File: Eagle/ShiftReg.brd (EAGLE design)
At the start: 100 x 100 mm, 206 parts, among them Q10 310mA/60V/1.6Ω, Q100 310mA/60V/1.6Ω, Q101 310mA/60V/1.6Ω, Q102 310mA/60V/1.6Ω, Q103 310mA/60V/1.6Ω, Q104 310mA/60V/1.6Ω, Q105 310mA/60V/1.6Ω, Q106 310mA/60V/1.6Ω, Q107 310mA/60V/1.6Ω, Q108 310mA/60V/1.6Ω, Q109 310mA/60V/1.6Ω, Q11 310mA/60V/1.6Ω, Q110 310mA/60V/1.6Ω, Q111 310mA/60V/1.6Ω, Q112 310mA/60V/1.6Ω, Q113 310mA/60V/1.6Ω, Q114 310mA/60V/1.6Ω, Q115 310mA/60V/1.6Ω, Q116 310mA/60V/1.6Ω, Q117 310mA/60V/1.6Ω, Q118 310mA/60V/1.6Ω, Q119 310mA/60V/1.6Ω, Q12 310mA/60V/1.6Ω, Q120 310mA/60V/1.6Ω, Q121 310mA/60V/1.6Ω, Q122 310mA/60V/1.6Ω, Q123 310mA/60V/1.6Ω, Q124 310mA/60V/1.6Ω, Q125 310mA/60V/1.6Ω, Q126 310mA/60V/1.6Ω, Q127 310mA/60V/1.6Ω, Q128 310mA/60V/1.6Ω, Q129 310mA/60V/1.6Ω, Q13 310mA/60V/1.6Ω, Q130 310mA/60V/1.6Ω, Q131 310mA/60V/1.6Ω, Q132 310mA/60V/1.6Ω, Q133 310mA/60V/1.6Ω, Q134 310mA/60V/1.6Ω, Q135 310mA/60V/1.6Ω, Q136 310mA/60V/1.6Ω, Q137 310mA/60V/1.6Ω, Q138 310mA/60V/1.6Ω, Q139 310mA/60V/1.6Ω, Q14 310mA/60V/1.6Ω, Q140 310mA/60V/1.6Ω, Q141 310mA/60V/1.6Ω, Q142 310mA/60V/1.6Ω, Q143 310mA/60V/1.6Ω, Q144 310mA/60V/1.6Ω, Q145 310mA/60V/1.6Ω, Q146 310mA/60V/1.6Ω, Q147 310mA/60V/1.6Ω, Q148 310mA/60V/1.6Ω, Q149 310mA/60V/1.6Ω, Q15 310mA/60V/1.6Ω, Q150 310mA/60V/1.6Ω, Q151 310mA/60V/1.6Ω, Q152 310mA/60V/1.6Ω, Q153 310mA/60V/1.6Ω, Q154 310mA/60V/1.6Ω, Q155 310mA/60V/1.6Ω, Q156 310mA/60V/1.6Ω, Q157 310mA/60V/1.6Ω, Q158 310mA/60V/1.6Ω, Q159 310mA/60V/1.6Ω, Q16 310mA/60V/1.6Ω, Q160 310mA/60V/1.6Ω, Q161 310mA/60V/1.6Ω, Q162 310mA/60V/1.6Ω, Q163 310mA/60V/1.6Ω, Q164 310mA/60V/1.6Ω, Q165 310mA/60V/1.6Ω, Q25 310mA/60V/1.6Ω, Q26 310mA/60V/1.6Ω, Q27 310mA/60V/1.6Ω, Q28 310mA/60V/1.6Ω, Q29 310mA/60V/1.6Ω, Q30 310mA/60V/1.6Ω, Q31 310mA/60V/1.6Ω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

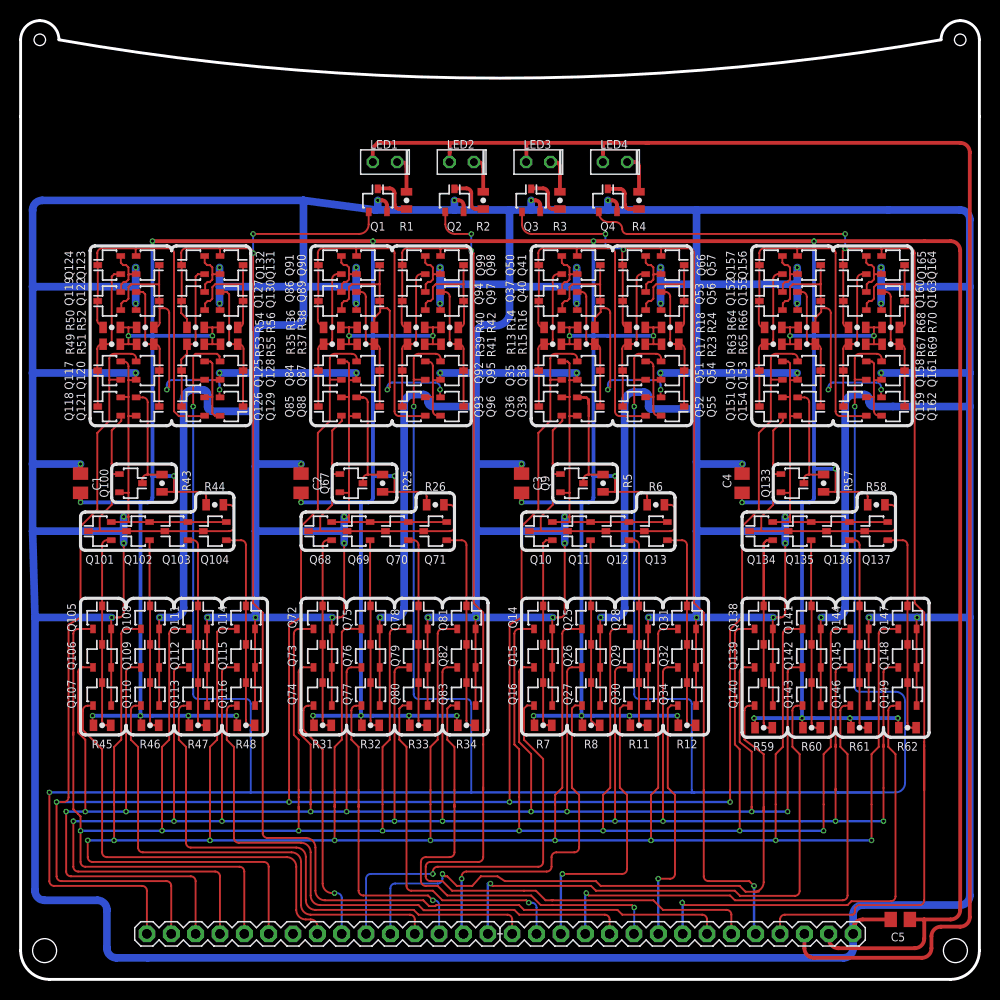
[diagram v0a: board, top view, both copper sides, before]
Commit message: Added clear to ShiftReg
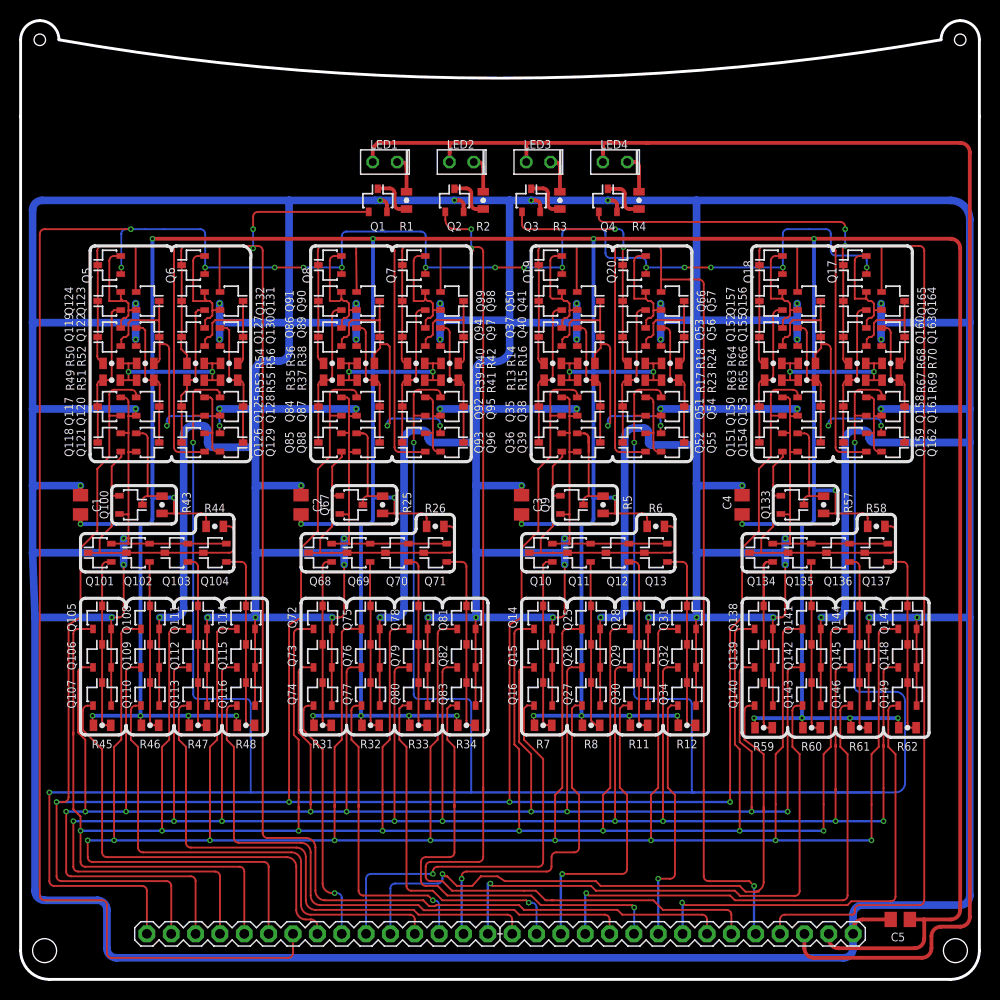
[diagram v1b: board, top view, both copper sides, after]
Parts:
- added Q17, Q18, Q19, Q20, Q5, Q6, Q7, Q8: 310mA/60V/1.6Ω, XSNOR:SOT23
- moved Q117 3.75 mm to (9.25, 59.5)
- moved Q118 3.75 mm to (9.25, 55.8)
- moved Q119 3.75 mm to (9.25, 66.8)
- moved Q120 3.75 mm to (13.2, 59.5)
- moved Q121 3.75 mm to (13.2, 55.8)
- moved Q122 3.75 mm to (13.2, 66.8)
- moved Q123 3.75 mm to (13.2, 70.5)
- moved Q124 3.75 mm to (9.25, 70.5)
- moved Q125 3.75 mm to (18.0, 59.5)
- moved Q126 3.75 mm to (18.0, 55.8)
- moved Q127 3.75 mm to (18.0, 66.8)
- moved Q128 3.75 mm to (22.0, 59.5)
- moved Q129 3.75 mm to (22.0, 55.8)
- moved Q130 3.75 mm to (22.0, 66.8)
- moved Q131 3.75 mm to (22.0, 70.5)
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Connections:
- new net CLR: JP2.7, Q17.1, Q18.1, Q19.1, Q20.1, Q5.1, Q6.1, Q7.1, Q8.1
- net GND: now also Q17.2, Q18.2, Q19.2, Q20.2, Q5.2, Q6.2, Q7.2, Q8.2
- net N$100: now also Q5.3
- net N$104: now also Q8.3
- net N$112: now also Q19.3
- net N$115: now also Q18.3
- net OUT0: now also Q6.3
- net OUT1: now also Q7.3
- net OUT2: now also Q20.3
- net OUT3: now also Q17.3
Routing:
- net CLR: track 0.00 -> 224.4 mm, vias 0 -> 15
- net GND: track 1333.8 -> 1354.1 mm
- net CLK: track 339.8 -> 324.8 mm
- net /CLK: track 308.0 -> 293.0 mm
- net N$112: track 37.4 -> 49.7 mm
- net N$104: track 37.4 -> 49.4 mm
- net N$100: track 37.4 -> 49.4 mm
- net N$115: track 37.3 -> 49.3 mm
- net OUT0: track 147.8 -> 157.4 mm
- net OUT1: track 129.7 -> 138.7 mm
- net OUT2: track 107.2 -> 112.5 mm
- net PREV3A': track 28.6 -> 24.1 mm
- net OUT3: track 136.0 -> 140.1 mm
- net R2A: track 15.1 -> 12.5 mm
- net PREV1A': track 20.6 -> 18.3 mm
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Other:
- board text added: "Clr"

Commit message: Shiftreg pcb have its own inverters for control signals
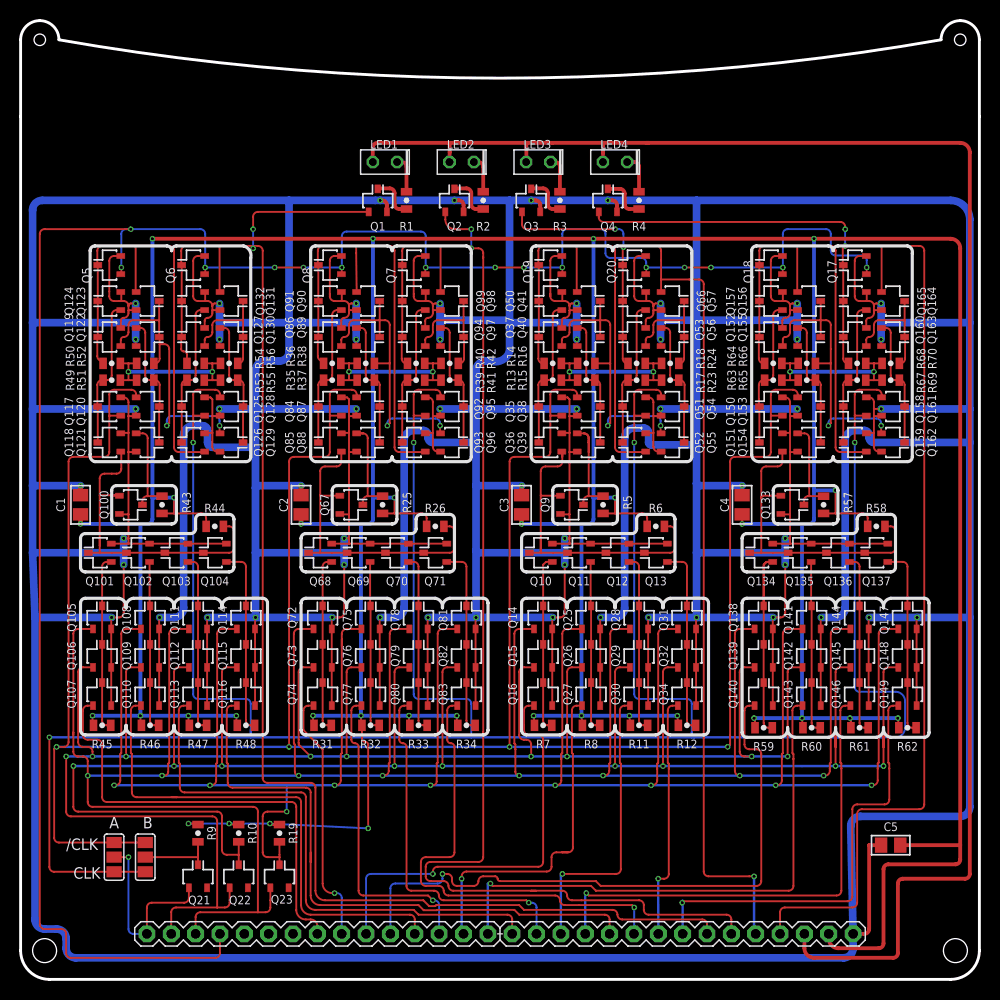
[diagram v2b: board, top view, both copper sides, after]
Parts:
- added Q21, Q22, Q23: 310mA/60V/1.6Ω, XSNOR:SOT23
- added R10, R19, R9: (no value), XSNOR:0805
- added SJ1, SJ2: (no value), jumper:SJ_2
- moved C5 7.81 mm to (90.8, 13.8)
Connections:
- new net CLK_IN: JP2.1, Q21.1, SJ2.2
- new net N$3: Q21.3, R9.1, SJ1.2
- net /CLK: now also SJ1.3, SJ2.3; no longer JP2.2
- net /OP1: now also Q22.3, R10.1; no longer JP2.4
- net /OP2: now also Q23.3, R19.1; no longer JP2.6
- net CLK: now also SJ1.1, SJ2.1; no longer JP2.1
- net CLR: now also JP2.4; no longer JP2.7
- net GND: now also Q21.2, Q22.2, Q23.2
- net OP1: now also JP2.2, Q22.1; no longer JP2.3
- net OP2: now also JP2.3, Q23.1; no longer JP2.5
- net VCC: now also R10.2, R19.2, R9.2
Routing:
- net /OP2: track 303.5 -> 241.0 mm
- net /OP1: track 250.3 -> 211.3 mm
- net VCC: track 597.2 -> 635.4 mm, vias 36 -> 40
- net OP1: track 233.8 -> 204.0 mm
- net OP2: track 289.9 -> 260.1 mm
- net CLK: track 324.8 -> 301.0 mm
- net /CLK: track 293.0 -> 271.1 mm
- net CLK_IN: track 0.00 -> 19.7 mm, vias 0 -> 1
- net N$3: track 0.00 -> 7.90 mm
- net CLR: track 224.4 -> 216.8 mm
- net GND: track 1354.1 -> 1360.6 mm
- net S2A: track 30.9 -> 34.8 mm
- net S0A-: track 30.9 -> 34.3 mm
- net S3A: track 30.9 -> 32.8 mm
- net S1A: track 30.9 -> 32.8 mm
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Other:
- board text added: "/CLK"
- board text added: "A"
- board text added: "B"
- board text added: "CLK"
